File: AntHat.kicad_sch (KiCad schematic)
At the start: 65 parts, among them J1 Raspberry_Pi_2_3, J2 0455580003, J3 PSU Comm, J4 61900411021, J5 61900411021, J6 0353180420, J7 0353180420, Q1 DMP3013SFV-7, U1 AP64501SP-13, U2 EMC2305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

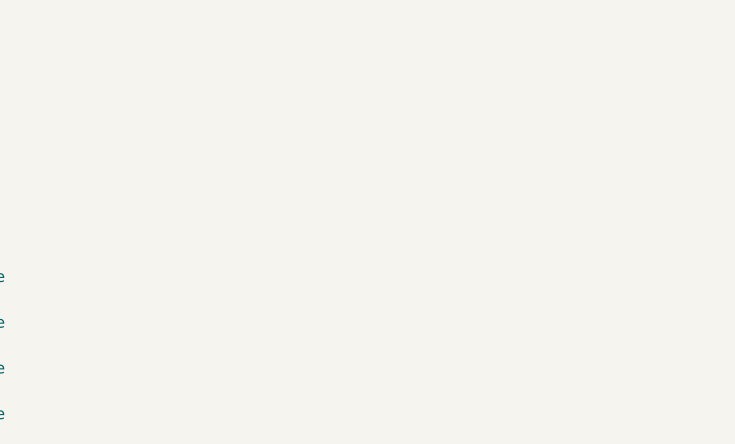
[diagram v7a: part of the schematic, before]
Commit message: added OSHWA logo. removed old gerbers
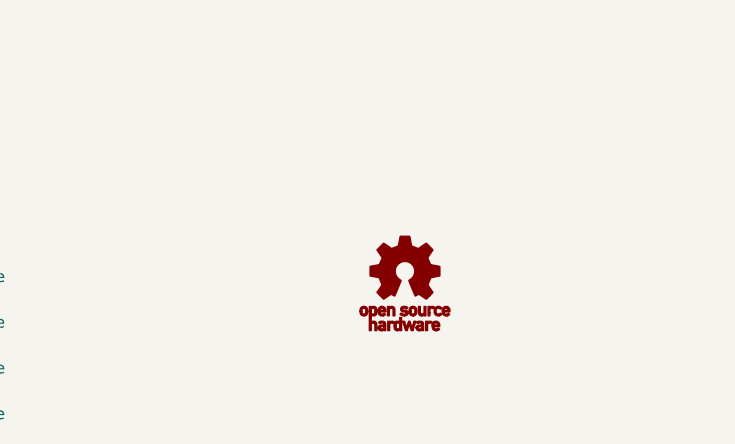
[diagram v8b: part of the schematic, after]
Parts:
- added G2: OSHWA-LOGO, AntHat:oshwa_logo, symbol AntHat:OSHWA-LOGO
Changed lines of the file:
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@@
+	)
+	(symbol
+		(lib_id "AntHat:OSHWA-LOGO")
+		(at 338.455 260.985 0)
+		(unit 1)
+		(exclude_from_sim no)
+		(in_bom yes)
+		(on_board yes)
+		(dnp no)
+		(fields_autoplaced yes)
+		(property "Reference" "G2"
+			(at 338.455 256.3622 0)
+			(effects
+				(font
+					(size 1.27 1.27)
+				)
+				(hide yes)
+			)
+		)
+		(property "Value" "OSHWA-LOGO"
+			(at 338.455 265.6078 0)
+			(effects
+				(font
+					(size 1.27 1.27)
+				)
+				(hide yes)
+			)
+		)
+		(property "Footprint" "AntHat:oshwa_logo"
+			(at 338.455 260.985 0)
+			(effects
+				(font
+					(size 1.27 1.27)
+				)
+				(hide yes)
+			)
+		)
+		(property "Datasheet" ""
+			(at 338.455 260.985 0)
+			(effects
+				(font
+					(size 1.27 1.27)
+				)
+				(hide yes)
+			)
+		)
+		(property "Description" ""
+			(at 338.455 260.985 0)
+			(effects
+				(font
+					(size 1.27 1.27)
+				)
+				(hide yes)
+			)
+		)
+		(instances
+			(project ""
+				(path "/8a5e5942-3c31-4d30-a0e0-705f88605e76"
+					(reference "G2")
+					(unit 1)
+				)
+			)
+		)
 	)
 	(symbol
